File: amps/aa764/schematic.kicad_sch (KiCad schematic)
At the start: 36 parts, among them T1 125P1B, T2 125A35A

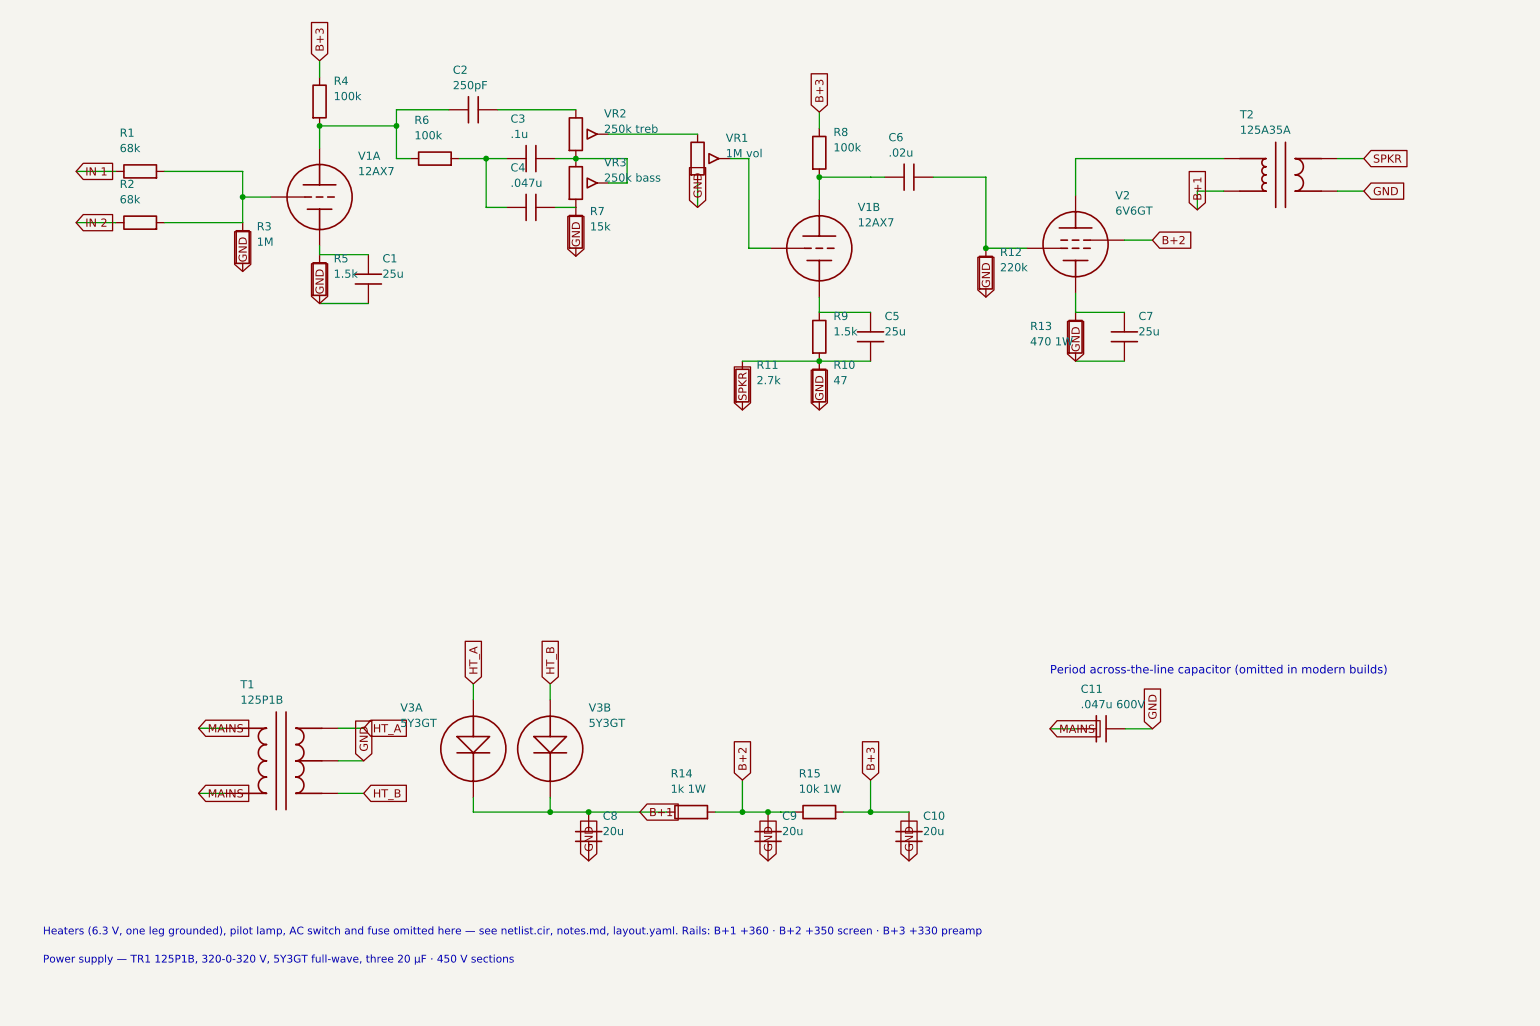
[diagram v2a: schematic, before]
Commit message: Fix: rotated global labels lettered their net names outside the flag
Every global label this pipeline emitted carried (justify left) regardless of
rotation. KiCanvas — like KiCad — draws label text horizontally at 0/180 and
vertically at 90/270 and reads WHICH SIDE of the anchor it letters on from the
justification, so at 180 and 270 the name printed outside an empty flag
outline, struck through by the very wire it names: 219 labels at 180 deg
(including the input-jack flags at top-left of nearly every sheet, the first
glyphs a visitor reads) and 792 GND/rail flags at 270 whose names squeezed at
the flag mouth instead of lettering down the body. The library already
compensated rotation for property text (`pa`); this mirrors that logic for
global labels: justify right at 180/270, left at 0/90.

check_schematics gains the geometry clause whose absence let all 1011
instances through a "no lettering through circuitry" pass: it modelled the
flag box but never the label TEXT, so a name rendered on the wrong side was
invisible to it. The gate now proves justification compensates rotation on
every global label.

Two more things this exposed, fixed in the same engine pass:

- Placement now measures with the renderer's own Newstroke advance table
  (extracted from the vendored kicanvas.js) instead of a flat 0.68-em prose
  average that under-read part lettering by a quarter — the mechanism behind
  every "metered clean, printed through its neighbour" incident. The GATE
  deliberately keeps the coarse ruler: re-ruling it with renderer truth was
  tried and red-flagged 28 of 34 sheets over abutments three visual passes
  had already judged sub-visual (the two-rulers note in schematic_lib.py).
- place_captions' escape ladder runs further, because a banner caption
  measured truly is half again wider than the old estimate believed.

All 34 schematics regenerated; full gate suite green.

🤖 Generated with [Claude Code](https://claude.com/claude-code)

Co-Authored-By: Claude Fable 5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
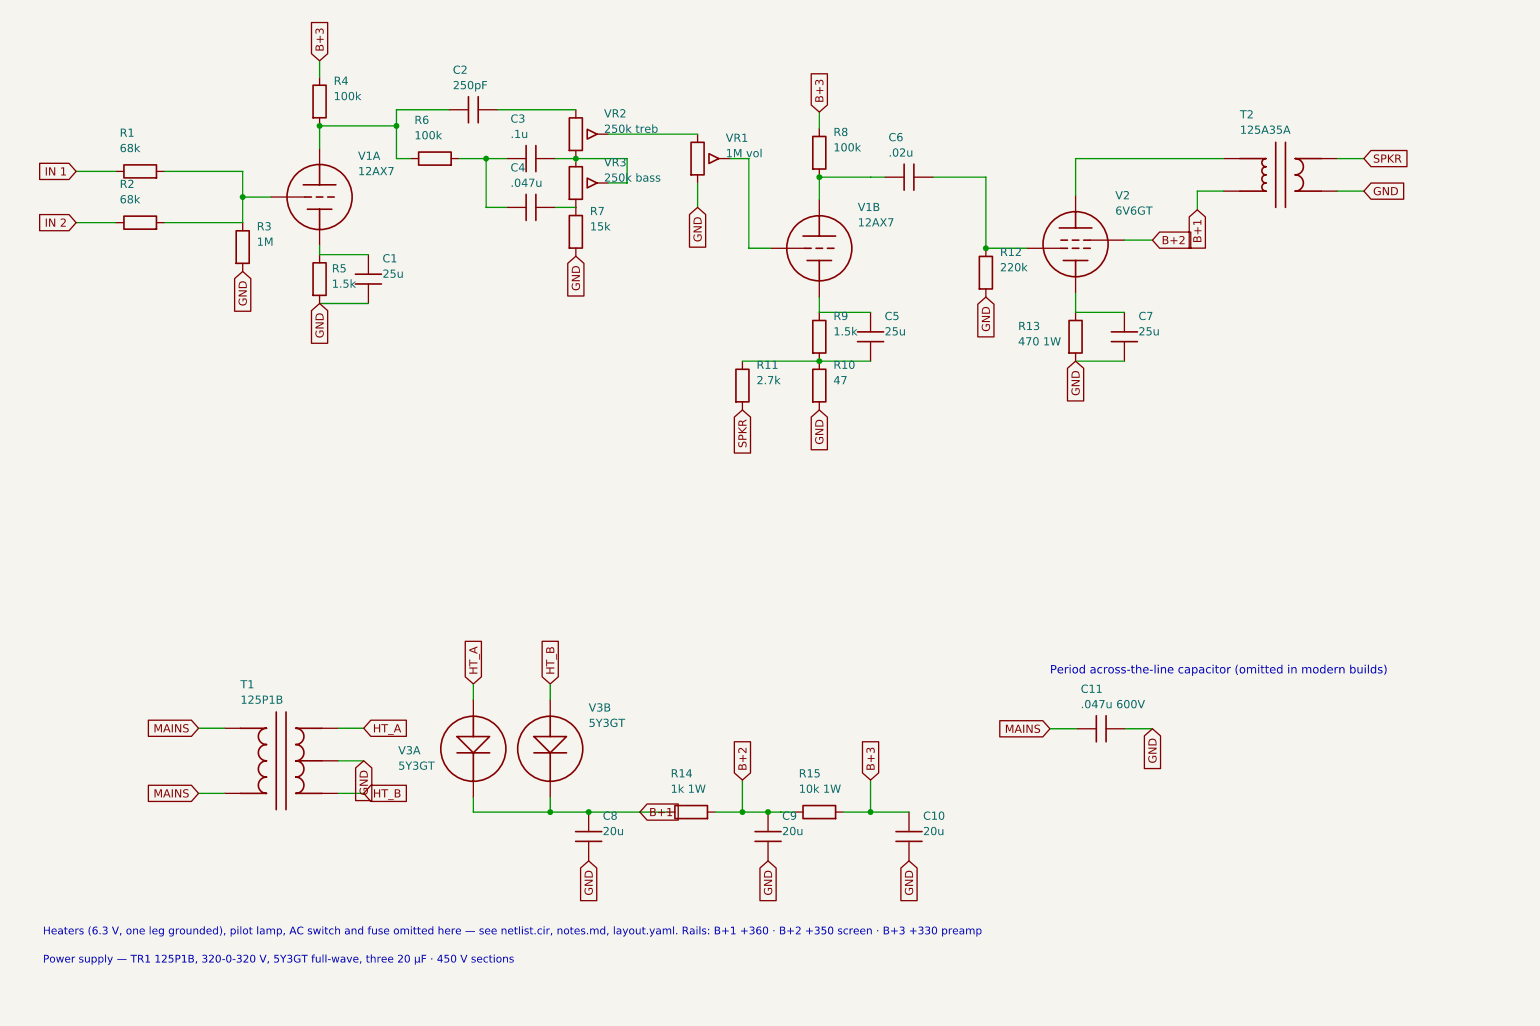
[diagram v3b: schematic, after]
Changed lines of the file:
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@@
     (comment 3 "Values read from: https://el34world.com/charts/Schematics/files/Fender/Fender_champ_AA764_schem.pdf"))
   (global_label "IN 1" (shape input) (at 17.8816 34.278 180)
-    (effects (font (size 1.27 1.27)) (justify left)))
+    (effects (font (size 1.27 1.27)) (justify right)))
   (global_label "IN 2" (shape input) (at 17.8816 42.278 180)
-    (effects (font (size 1.27 1.27)) (justify left)))
+    (effects (font (size 1.27 1.27)) (justify right)))
   (symbol (lib_id "cx:R") (at 27.8816 34.278 90) (unit 1)
     (in_bom yes) (on_board yes)
@@
     (property "Value" "1M" (at 46.0816 45.288 0) (effects (font (size 1.27 1.27)) (justify left))))
   (global_label "GND" (shape input) (at 43.8816 49.898 270)
-    (effects (font (size 1.27 1.27)) (justify left)))
+    (effects (font (size 1.27 1.27)) (justify right)))
   (symbol (lib_id "cx:TRIODE") (at 55.8816 38.278 0) (unit 1)
     (in_bom yes) (on_board yes)
@@
   (symbol (lib_id "cx:R") (at 55.8816 51.088 0) (unit 1)
     (in_bom yes) (on_board yes)
-    (property "Reference" "R5" (at 58.0816 47.888 0) (effects (font (size 1.27 1.27)) (justify left)))
-    (property "Value" "1.5k" (at 58.0816 50.288 0) (effects (font (size 1.27 1.27)) (justify left))))
+    (property "Reference" "R5" (at 57.7976 49.448 0) (effects (font (size 1.27 1.27)) (justify left)))
+    (property "Value" "1.5k" (at 57.7976 51.848 0) (effects (font (size 1.27 1.27)) (justify left))))
   (symbol (lib_id "cx:C") (at 63.5016 51.088 0) (unit 1)
     (in_bom yes) (on_board yes)
@@
     (stroke (width 0) (type default)))
   (global_label "GND" (shape input) (at 55.8816 54.898 270)
-    (effects (font (size 1.27 1.27)) (justify left)))
+    (effects (font (size 1.27 1.27)) (justify right)))
   (junction (at 55.8816 27.178) (diameter 0) (color 0 0 0 0))
   (wire (pts (xy 55.8816 27.178) (xy 67.8816 27.178))
@@
     (property "Value" "15k" (at 98.0816 42.908 0) (effects (font (size 1.27 1.27)) (justify left))))
   (global_label "GND" (shape input) (at 95.8816 47.518 270)
-    (effects (font (size 1.27 1.27)) (justify left)))
+    (effects (font (size 1.27 1.27)) (justify right)))
   (wire (pts (xy 100.962 28.468) (xy 114.882 28.468))
     (stroke (width 0) (type default)))
@@
     (stroke (width 0) (type default)))
   (global_label "GND" (shape input) (at 114.882 39.898 270)
-    (effects (font (size 1.27 1.27)) (justify left)))
+    (effects (font (size 1.27 1.27)) (justify right)))
   (symbol (lib_id "cx:TRIODE") (at 133.882 46.278 0) (unit 1)
     (in_bom yes) (on_board yes)
@@
     (property "Value" "47" (at 136.082 66.908 0) (effects (font (size 1.27 1.27)) (justify left))))
   (global_label "GND" (shape input) (at 133.882 71.518 270)
-    (effects (font (size 1.27 1.27)) (justify left)))
+    (effects (font (size 1.27 1.27)) (justify right)))
   (wire (pts (xy 121.882 63.898) (xy 133.882 63.898))
     (stroke (width 0) (type default)))
@@
     (property "Value" "2.7k" (at 124.082 66.908 0) (effects (font (size 1.27 1.27)) (justify left))))
   (global_label "SPKR" (shape input) (at 121.882 71.518 270)
-    (effects (font (size 1.27 1.27)) (justify left)))
+    (effects (font (size 1.27 1.27)) (justify right)))
   (junction (at 133.882 35.178) (diameter 0) (color 0 0 0 0))
   (wire (pts (xy 133.882 35.178) (xy 141.882 35.178))
@@
     (property "Value" "220k" (at 162.082 49.288 0) (effects (font (size 1.27 1.27)) (justify left))))
   (global_label "GND" (shape input) (at 159.882 53.898 270)
-    (effects (font (size 1.27 1.27)) (justify left)))
+    (effects (font (size 1.27 1.27)) (justify right)))
   (symbol (lib_id "cx:PENTODE") (at 173.882 45.643 0) (unit 1)
     (in_bom yes) (on_board yes)
@@
   (symbol (lib_id "cx:R") (at 173.882 60.088 0) (unit 1)
     (in_bom yes) (on_board yes)
-    (property "Reference" "R13" (at 166.784 58.448 0) (effects (font (size 1.27 1.27)) (justify left)))
-    (property "Value" "470 1W" (at 166.784 60.848 0) (effects (font (size 1.27 1.27)) (justify left))))
+    (property "Reference" "R13" (at 164.916 58.448 0) (effects (font (size 1.27 1.27)) (justify left)))
+    (property "Value" "470 1W" (at 164.916 60.848 0) (effects (font (size 1.27 1.27)) (justify left))))
   (symbol (lib_id "cx:C") (at 181.502 60.088 0) (unit 1)
     (in_bom yes) (on_board yes)
@@
     (stroke (width 0) (type default)))
   (global_label "GND" (shape input) (at 173.882 63.898 270)
-    (effects (font (size 1.27 1.27)) (justify left)))
+    (effects (font (size 1.27 1.27)) (justify right)))
   (wire (pts (xy 173.882 38.023) (xy 173.882 32.278))
     (stroke (width 0) (type default)))
@@
     (stroke (width 0) (type default)))
   (global_label "B+1" (shape input) (at 192.882 40.278 270)
-    (effects (font (size 1.27 1.27)) (justify left)))
+    (effects (font (size 1.27 1.27)) (justify right)))
   (wire (pts (xy 214.772 32.278) (xy 218.882 32.278))
     (stroke (width 0) (type default)))
@@
     (stroke (width 0) (type default)))
   (global_label "MAINS" (shape input) (at 36.9916 121.198 180)
-    (effects (font (size 1.27 1.27)) (justify left)))
+    (effects (font (size 1.27 1.27)) (justify right)))
   (wire (pts (xy 40.9916 131.358) (xy 36.9916 131.358))
     (stroke (width 0) (type default)))
   (global_label "MAINS" (shape input) (at 36.9916 131.358 180)
-    (effects (font (size 1.27 1.27)) (justify left)))
+    (effects (font (size 1.27 1.27)) (justify right)))
   (wire (pts (xy 58.7716 121.198) (xy 62.7716 121.198))
     (stroke (width 0) (type default)))
@@
     (stroke (width 0) (type default)))
   (global_label "GND" (shape input) (at 62.7716 126.278 270)
-    (effects (font (size 1.27 1.27)) (justify left)))
+    (effects (font (size 1.27 1.27)) (justify right)))
   (global_label "HT_A" (shape input) (at 79.8816 114.278 90)
     (effects (font (size 1.27 1.27)) (justify left)))
@@
   (symbol (lib_id "cx:DIODE_TUBE") (at 79.8816 124.398 0) (unit 1)
     (in_bom yes) (on_board yes)
-    (property "Reference" "V3A" (at 68.4816 117.998 0) (effects (font (size 1.27 1.27)) (justify left)))
-    (property "Value" "5Y3GT" (at 68.4816 120.398 0) (effects (font (size 1.27 1.27)) (justify left))))
+    (property "Reference" "V3A" (at 68.1574 124.678 0) (effects (font (size 1.27 1.27)) (justify left)))
+    (property "Value" "5Y3GT" (at 68.1574 127.078 0) (effects (font (size 1.27 1.27)) (justify left))))
   (global_label "HT_B" (shape input) (at 91.8816 114.278 90)
     (effects (font (size 1.27 1.27)) (justify left)))
@@
     (property "Value" "20u" (at 100.082 137.288 0) (effects (font (size 1.27 1.27)) (justify left))))
   (global_label "GND" (shape input) (at 97.8816 141.898 270)
-    (effects (font (size 1.27 1.27)) (justify left)))
+    (effects (font (size 1.27 1.27)) (justify right)))
   (global_label "B+1" (shape input) (at 105.882 134.278 0)
     (effects (font (size 1.27 1.27)) (justify left)))
@@
     (property "Value" "20u" (at 128.082 137.288 0) (effects (font (size 1.27 1.27)) (justify left))))
   (global_label "GND" (shape input) (at 125.882 141.898 270)
-    (effects (font (size 1.27 1.27)) (justify left)))
+    (effects (font (size 1.27 1.27)) (justify right)))
   (wire (pts (xy 127.882 134.278) (xy 130.072 134.278))
     (stroke (width 0) (type default)))
@@
     (property "Value" "20u" (at 150.082 137.288 0) (effects (font (size 1.27 1.27)) (justify left))))
   (global_label "GND" (shape input) (at 147.882 141.898 270)
-    (effects (font (size 1.27 1.27)) (justify left)))
+    (effects (font (size 1.27 1.27)) (justify right)))
   (text "Period across-the-line capacitor (omitted in modern builds)" (at 169.882 112.278 0)
     (effects (font (size 1.3 1.3)) (justify left)))
   (global_label "MAINS" (shape input) (at 169.882 121.278 180)
-    (effects (font (size 1.27 1.27)) (justify left)))
+    (effects (font (size 1.27 1.27)) (justify right)))
   (wire (pts (xy 169.882 121.278) (xy 174.072 121.278))
     (stroke (width 0) (type default)))
@@
     (stroke (width 0) (type default)))
   (global_label "GND" (shape input) (at 185.882 121.278 270)
-    (effects (font (size 1.27 1.27)) (justify left)))
+    (effects (font (size 1.27 1.27)) (justify right)))
   (text "Heaters (6.3 V, one leg grounded), pilot lamp, AC switch and fuse omitted here — see netlist.cir, notes.md, layout.yaml. Rails: B+1 +360 · B+2 +350 screen · B+3 +330 preamp" (at 12.7 153.056 0)
     (effects (font (size 1.2 1.2)) (justify left)))

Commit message: Fix: deterministic schematic ids and wires split at every join
- _u() is uuid5 over (amp id, emission order), so a regeneration of an
  unchanged script is byte-identical and a drift gate becomes possible
- write() splits wire segments at symbol pins, wire ends and junction dots,
  so the file connects exactly what the drawing shows under KiCad's
  endpoint-only semantics (270 pins were on a wire's interior; net
  partitions unchanged on all 38 sheets)
- all sheets regenerated; aa864-bassman title block was stale (draft) and
  now matches meta.yaml (verified)

Co-Authored-By: Claude Fable 5.1 <noreply@anthropic.com>
Claude-Session: https://claude.ai/code/session_01KBMfdh37HmCL2iWcBiL5J1
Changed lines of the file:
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@@
   (wire (pts (xy 31.6916 42.278) (xy 43.8816 42.278))
     (stroke (width 0) (type default)))
-  (wire (pts (xy 43.8816 34.278) (xy 43.8816 42.278))
+  (wire (pts (xy 43.8816 34.278) (xy 43.8816 38.278))
+    (stroke (width 0) (type default)))
+  (wire (pts (xy 43.8816 38.278) (xy 43.8816 42.278))
     (stroke (width 0) (type default)))
   (junction (at 43.8816 38.278) (diameter 0) (color 0 0 0 0))
@@
   (wire (pts (xy 55.8816 27.178) (xy 67.8816 27.178))
     (stroke (width 0) (type default)))
-  (wire (pts (xy 67.8816 24.658) (xy 67.8816 32.278))
+  (wire (pts (xy 67.8816 24.658) (xy 67.8816 27.178))
+    (stroke (width 0) (type default)))
+  (wire (pts (xy 67.8816 27.178) (xy 67.8816 32.278))
     (stroke (width 0) (type default)))
   (junction (at 67.8816 27.178) (diameter 0) (color 0 0 0 0))
@@
   (wire (pts (xy 91.8816 132.018) (xy 91.8816 134.278))
     (stroke (width 0) (type default)))
-  (wire (pts (xy 79.8816 134.278) (xy 105.882 134.278))
+  (wire (pts (xy 79.8816 134.278) (xy 91.8816 134.278))
+    (stroke (width 0) (type default)))
+  (wire (pts (xy 91.8816 134.278) (xy 97.8816 134.278))
+    (stroke (width 0) (type default)))
+  (wire (pts (xy 97.8816 134.278) (xy 105.882 134.278))
     (stroke (width 0) (type default)))
   (junction (at 91.8816 134.278) (diameter 0) (color 0 0 0 0))
@@
     (property "Reference" "R14" (at 110.682 128.278 270) (effects (font (size 1.27 1.27)) (justify left)))
     (property "Value" "1k 1W" (at 110.682 130.678 270) (effects (font (size 1.27 1.27)) (justify left))))
-  (wire (pts (xy 117.692 134.278) (xy 127.882 134.278))
+  (wire (pts (xy 117.692 134.278) (xy 121.882 134.278))
+    (stroke (width 0) (type default)))
+  (wire (pts (xy 121.882 134.278) (xy 125.882 134.278))
+    (stroke (width 0) (type default)))
+  (wire (pts (xy 125.882 134.278) (xy 127.882 134.278))
     (stroke (width 0) (type default)))
   (junction (at 121.882 134.278) (diameter 0) (color 0 0 0 0))
@@
     (property "Reference" "R15" (at 130.682 128.278 270) (effects (font (size 1.27 1.27)) (justify left)))
     (property "Value" "10k 1W" (at 130.682 130.678 270) (effects (font (size 1.27 1.27)) (justify left))))
-  (wire (pts (xy 137.692 134.278) (xy 147.882 134.278))
+  (wire (pts (xy 137.692 134.278) (xy 141.882 134.278))
+    (stroke (width 0) (type default)))
+  (wire (pts (xy 141.882 134.278) (xy 147.882 134.278))
     (stroke (width 0) (type default)))
   (junction (at 141.882 134.278) (diameter 0) (color 0 0 0 0))
